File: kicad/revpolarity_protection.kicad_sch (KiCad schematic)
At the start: 5 parts

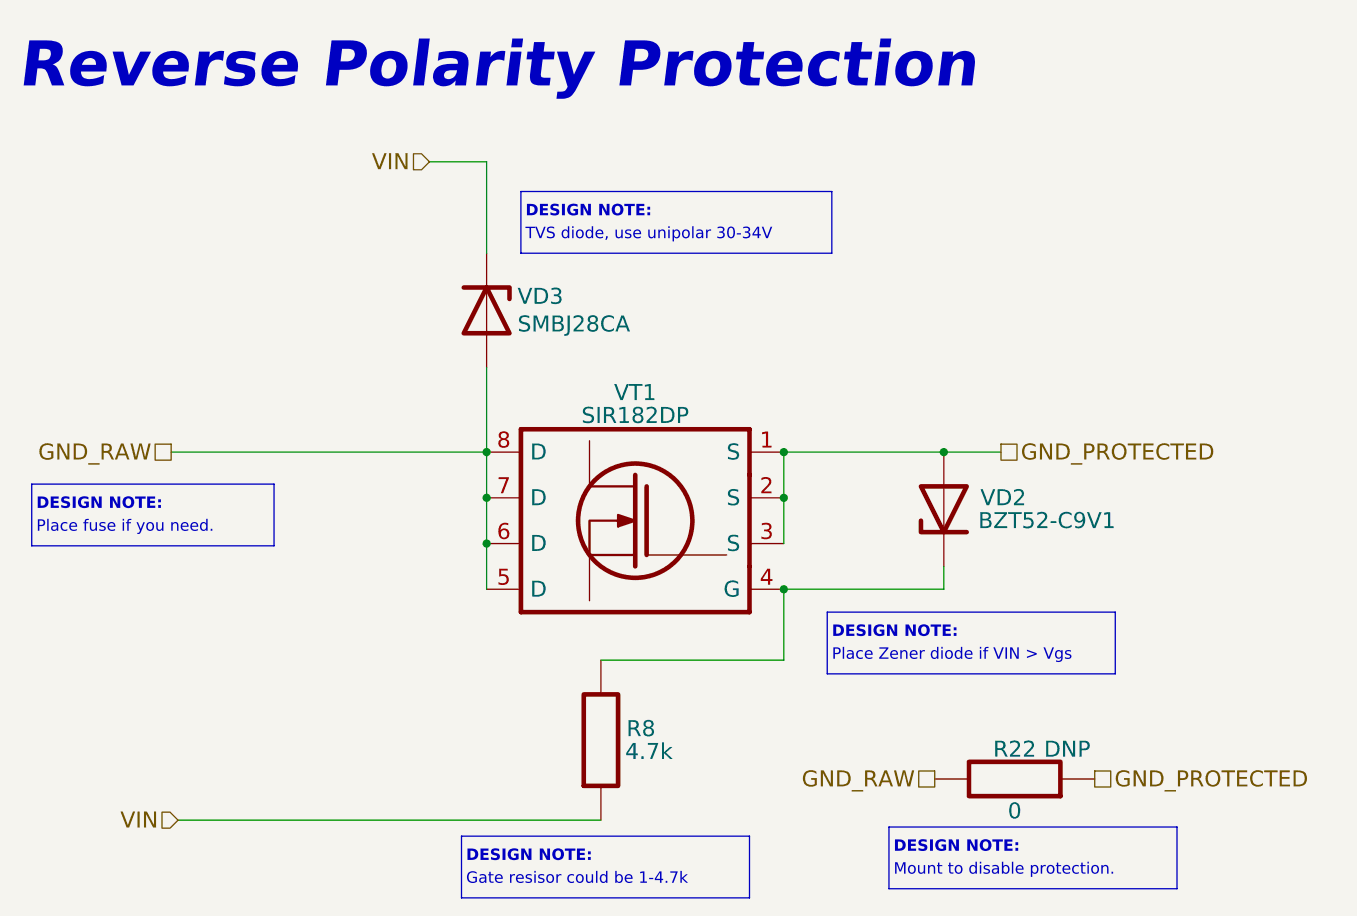
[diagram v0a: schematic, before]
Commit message: Reannotate schematic; Fix 5032 crystal footprint field; Update PCB with 5032 crystal
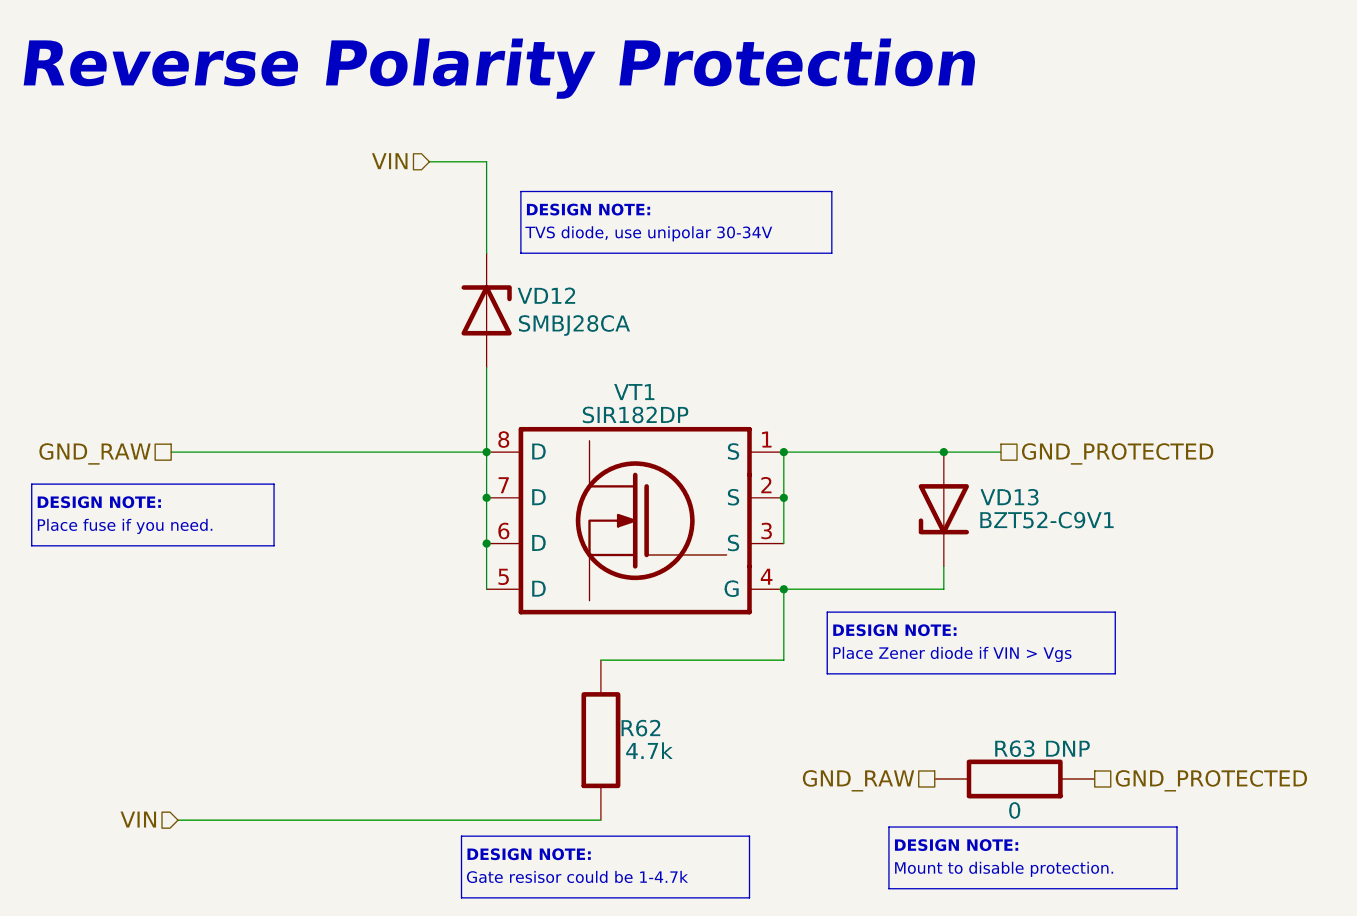
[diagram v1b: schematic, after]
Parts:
- renumbered R8 to R62, R22 to R63, VD3 to VD12, VD2 to VD13
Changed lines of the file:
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@@
   (symbol (lib_id "Diodes:VD_ZENER") (at 195.326 100.838 270) (unit 1)
     (in_bom yes) (on_board yes)
-    (property "Reference" "VD2" (id 0) (at 199.39 99.568 90)
+    (property "Reference" "VD13" (id 0) (at 199.39 99.568 90)
       (effects (font (size 1.778 1.778)) (justify left))
     )
@@
   (symbol (lib_id "Resistors:R_RES") (at 203.2 130.81 180) (unit 1)
     (in_bom yes) (on_board yes)
-    (property "Reference" "R22" (id 0) (at 203.2 127.508 0)
+    (property "Reference" "R63" (id 0) (at 203.2 127.508 0)
       (effects (font (size 1.778 1.778)))
     )
@@
   (symbol (lib_id "Diodes:D_ZENER_SPICE") (at 144.526 78.74 90) (unit 1)
     (in_bom yes) (on_board yes)
-    (property "Reference" "VD3" (id 0) (at 147.955 77.1906 90)
+    (property "Reference" "VD12" (id 0) (at 147.955 77.1906 90)
       (effects (font (size 1.778 1.778)) (justify right))
     )
@@
   (symbol (lib_id "Resistors:R_RES") (at 157.226 126.492 90) (unit 1)
     (in_bom yes) (on_board yes)
-    (property "Reference" "R8" (id 0) (at 161.671 125.222 90)
+    (property "Reference" "R62" (id 0) (at 161.671 125.222 90)
       (effects (font (size 1.778 1.778)))
     )

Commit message: Add voltage value to caps, update BOM, SCH, ASM
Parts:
- R62, R63: Case/Package 0000 -> 0603; Tolerance ±% -> ±5%
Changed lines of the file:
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@@
       (effects (font (size 1.778 1.778)))
     )
-    (property "Case/Package" "0000" (id 5) (at 203.2 124.46 0)
+    (property "Case/Package" "0603" (id 5) (at 203.2 124.46 0)
       (effects (font (size 1.27 1.27)) hide)
     )
@@
       (effects (font (size 1.27 1.27)) hide)
     )
-    (property "Tolerance" "±%" (id 7) (at 203.2 121.158 0)
+    (property "Tolerance" "±5%" (id 7) (at 203.2 121.158 0)
       (effects (font (size 1.27 1.27)) hide)
     )
+    (property "Part Number" "" (id 8) (at 203.2 130.81 0))
     (pin "1")
     (pin "2")
@@
     (pin "2")
   )
-  (symbol (lib_id "Resistors:R_RES") (at 157.226 126.492 90) (unit 1)
+  (symbol (lib_name "R_RES_1") (lib_id "Resistors:R_RES") (at 157.226 126.492 90) (unit 1)
     (in_bom yes) (on_board yes)
     (property "Reference" "R62" (id 0) (at 161.671 125.222 90)
@@
       (effects (font (size 1.778 1.778)))
     )
-    (property "Case/Package" "0000" (id 5) (at 163.576 126.492 0)
+    (property "Case/Package" "0603" (id 5) (at 163.576 126.492 0)
       (effects (font (size 1.27 1.27)) hide)
     )
@@
       (effects (font (size 1.27 1.27)) hide)
     )
-    (property "Tolerance" "±%" (id 7) (at 166.878 126.492 0)
+    (property "Tolerance" "±5%" (id 7) (at 166.878 126.492 0)
       (effects (font (size 1.27 1.27)) hide)
     )
+    (property "Part Number" "" (id 8) (at 157.226 126.492 0))
     (pin "1")
     (pin "2")

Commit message: Add wiring diagram; Add work ours (stage 2); refactor folders
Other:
- title: (none) -> RadioSens v1
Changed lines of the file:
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@@
 (kicad_sch (version 20211123) (generator eeschema)
   (paper "A4")
+  (title_block
+    (title "RadioSens v1")
+    (comment 2 "Electrical Circuit")
+  )
   (junction (at 177.546 99.568) (diameter 0) (color 0 0 0 0)
   )
